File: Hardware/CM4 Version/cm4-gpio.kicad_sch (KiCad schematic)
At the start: 2 parts, among them J1 UART

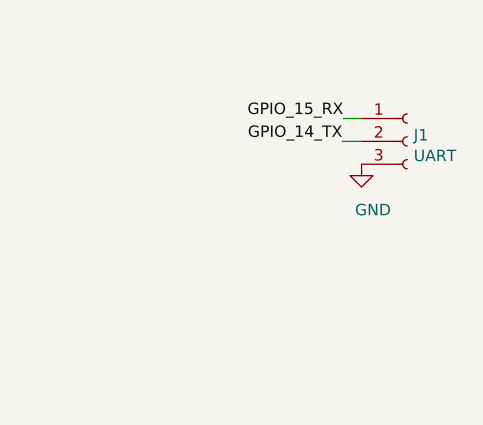
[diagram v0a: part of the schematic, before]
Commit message: Remove CM4-Backups
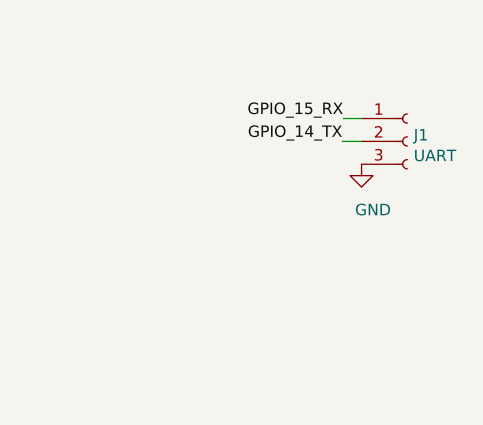
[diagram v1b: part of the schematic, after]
